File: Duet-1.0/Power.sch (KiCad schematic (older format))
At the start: 25 parts, among them J21 12V_ref, J30 5V_ref, J31 3v3_ref, U2 TC2117-3.3VDBTR, U3 MC7805CDTG

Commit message: Work-in-progress: Adding JMG's clean 5V buck converter.
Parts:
- removed U3: MC7805CDTG, symbol 7805
- added C96: 100u, symbol C
- added D19: SS14M, symbol DIODESCH
- added L1: L_MINI, ~, symbol L_MINI
- added U3: LM2596, symbol LM2596
- C3: value 100u -> 470u
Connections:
- wire segments 55 -> 60
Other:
- note added: "12-24V Input, 5V 2A Output buck converter\n"
- note removed: "12-24V Input, 5V 1A Output 7805 regulator\n"
- moved on the sheet: C3, C5, D1, D13, D14, D2, JP1, JP9
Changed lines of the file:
@@
 LIBS:FE
 LIBS:Shield-cache
+LIBS:emaker
+LIBS:SparkFun
 LIBS:Duet1.0-cache
 EELAYER 27 0
@@
 Wire Wire Line
 	6000 4900 6000 4800
-Connection ~ 5250 1800
-Wire Wire Line
-	5250 1800 5250 1900
-Wire Wire Line
-	4100 2100 4100 2200
-Wire Wire Line
-	2600 1800 2250 1800
+Connection ~ 6150 1800
+Wire Wire Line
+	6150 1800 6150 1900
 Wire Wire Line
 	6600 4450 6600 4050
@@
 Wire Notes Line
 	5000 3650 7000 3650
-Wire Wire Line
-	5950 1300 5700 1300
-Connection ~ 5700 1800
-Wire Wire Line
-	5700 1300 5700 1800
 Wire Wire Line
 	2000 5450 2000 5550
@@
 Connection ~ 3250 4250
 Wire Wire Line
-	5250 2550 5250 2300
-Wire Wire Line
-	3200 2200 3200 3000
+	6150 2550 6150 2300
+Wire Wire Line
+	2500 2200 2500 3000
 Wire Wire Line
 	6600 5500 6600 5150
-Wire Wire Line
-	4600 1800 4500 1800
 Wire Wire Line
 	6150 4800 5850 4800
@@
 	6000 5400 6600 5400
 Connection ~ 6600 5400
-Connection ~ 3200 2800
 Wire Wire Line
 	2150 5000 2150 5450
@@
 Connection ~ 4250 4250
 Wire Wire Line
-	1750 1800 1850 1800
-Connection ~ 1800 1800
-Wire Wire Line
-	4100 2200 3200 2200
-Connection ~ 3550 2200
-Wire Wire Line
-	3700 1800 3200 1800
-Connection ~ 3550 1800
+	1650 2300 1650 2200
+Connection ~ 1650 2250
+Connection ~ 2850 1800
 $Comp
 L C C95
@@
 L CP1 C5
 U 1 1 53B02FA8
-P 3550 2000
-F 0 "C5" H 3600 2100 50  0000 L CNN
-F 1 "0u33" H 3600 1900 50  0000 L CNN
-F 2 "" H 3550 2000 60  0001 C CNN
-F 3 "" H 3550 2000 60  0001 C CNN
-	1    3550 2000
+P 2850 2000
+F 0 "C5" H 2900 2100 50  0000 L CNN
+F 1 "0u33" H 2900 1900 50  0000 L CNN
+F 2 "" H 2850 2000 60  0001 C CNN
+F 3 "" H 2850 2000 60  0001 C CNN
+	1    2850 2000
 	1    0    0    -1
 $EndComp
@@
 L DIODESCH D2
 U 1 1 53B02782
-P 4800 1800
-F 0 "D2" H 4800 1900 40  0000 C CNN
-F 1 "SS14M" H 4800 1700 40  0000 C CNN
-F 2 "" H 4800 1800 60  0001 C CNN
-F 3 "" H 4800 1800 60  0001 C CNN
-	1    4800 1800
-	1    0    0    -1
-$EndComp
-$Comp
-L 7805 U3
-U 1 1 53B01DB6
-P 4100 1850
-F 0 "U3" H 4250 1654 60  0000 C CNN
-F 1 "MC7805CDTG" H 4100 2050 60  0000 C CNN
-F 2 "" H 4100 1850 60  0001 C CNN
-F 3 "" H 4100 1850 60  0001 C CNN
-	1    4100 1850
+P 5850 1800
+F 0 "D2" H 5850 1900 40  0000 C CNN
+F 1 "SS14M" H 5850 1700 40  0000 C CNN
+F 2 "" H 5850 1800 60  0001 C CNN
+F 3 "" H 5850 1800 60  0001 C CNN
+	1    5850 1800
 	1    0    0    -1
 $EndComp
@@
 Text GLabel 6150 4050 0    60   Input ~ 0
 PS_ON_IN
-Text Notes 5400 2150 0    60   ~ 0
+Text Notes 6300 2150 0    60   ~ 0
 1A
 Text Notes 6000 3250 0    60   ~ 0
@@
 L JUMPER JP9
 U 1 1 52209EAB
-P 2900 1800
-F 0 "JP9" H 2900 1950 60  0000 C CNN
-F 1 "5V_EN" H 2900 1720 40  0000 C CNN
-F 2 "" H 2900 1800 60  0001 C CNN
-F 3 "" H 2900 1800 60  0001 C CNN
-	1    2900 1800
+P 2100 1800
+F 0 "JP9" H 2100 1950 60  0000 C CNN
+F 1 "5V_EN" H 2100 1720 40  0000 C CNN
+F 2 "" H 2100 1800 60  0001 C CNN
+F 3 "" H 2100 1800 60  0001 C CNN
+	1    2100 1800
 	1    0    0    -1
 $EndComp
@@
 L SS3P4 D1
 U 1 1 5116BBAA
-P 2050 1800
-F 0 "D1" H 2050 1900 40  0000 C CNN
-F 1 "SS3P4" H 2050 1700 40  0000 C CNN
-F 2 "" H 2050 1800 60  0001 C CNN
-F 3 "" H 2050 1800 60  0001 C CNN
-	1    2050 1800
-	1    0    0    -1
+P 1650 2000
+F 0 "D1" H 1650 2100 40  0000 C CNN
+F 1 "SS3P4" H 1650 1900 40  0000 C CNN
+F 2 "" H 1650 2000 60  0001 C CNN
+F 3 "" H 1650 2000 60  0001 C CNN
+	1    1650 2000
+	0    -1   -1   0
 $EndComp
 $Comp
 L DIODESCH D13
 U 1 1 50F99BAC
-P 5250 2100
-F 0 "D13" H 5250 2200 40  0000 C CNN
-F 1 "SS14M" H 5250 2000 40  0000 C CNN
-F 2 "" H 5250 2100 60  0001 C CNN
-F 3 "" H 5250 2100 60  0001 C CNN
-	1    5250 2100
+P 6150 2100
+F 0 "D13" H 6150 2200 40  0000 C CNN
+F 1 "SS14M" H 6150 2000 40  0000 C CNN
+F 2 "" H 6150 2100 60  0001 C CNN
+F 3 "" H 6150 2100 60  0001 C CNN
+	1    6150 2100
 	0    -1   -1   0
 $EndComp
-Text GLabel 5250 2550 3    60   Input ~ 0
+Text GLabel 6150 2550 3    60   Input ~ 0
 VBUS
 $Comp
@@
 5V Input, 3.3V 500mA Output\nLow Drop-Out Linear Regulator
 Text Notes 1500 1300 0    60   ~ 0
-12-24V Input, 5V 1A Output 7805 regulator\n
+12-24V Input, 5V 2A Output buck converter\n
 Text GLabel 4350 4250 2    60   Input ~ 0
 +3.3V
 Text GLabel 1800 4250 0    60   Input ~ 0
 +5V
-Text GLabel 1750 1800 0    60   Input ~ 0
+Text GLabel 1650 2300 3    60   Input ~ 0
 V_IN
-Text GLabel 5950 1300 2    60   Input ~ 0
+Text GLabel 6650 1300 2    60   Input ~ 0
 +5V
 $Comp
@@
 L GND #PWR31
 U 1 1 50522566
-P 3200 3000
-F 0 "#PWR31" H 3200 3000 30  0001 C CNN
-F 1 "GND" H 3200 2930 30  0001 C CNN
-F 2 "" H 3200 3000 60  0001 C CNN
-F 3 "" H 3200 3000 60  0001 C CNN
-	1    3200 3000
+P 2500 3000
+F 0 "#PWR31" H 2500 3000 30  0001 C CNN
+F 1 "GND" H 2500 2930 30  0001 C CNN
+F 2 "" H 2500 3000 60  0001 C CNN
+F 3 "" H 2500 3000 60  0001 C CNN
+	1    2500 3000
 	1    0    0    -1
 $EndComp
@@
 L C C3
 U 1 1 50522565
-P 3200 2000
-F 0 "C3" H 3250 2100 50  0000 L CNN
-F 1 "100u" H 3250 1900 50  0000 L CNN
-F 2 "" H 3200 2000 60  0001 C CNN
-F 3 "" H 3200 2000 60  0001 C CNN
-F 4 "35V" H 3250 1830 50  0000 L CNN "Voltage"
-	1    3200 2000
+P 2500 2000
+F 0 "C3" H 2550 2100 50  0000 L CNN
+F 1 "470u" H 2550 1900 50  0000 L CNN
+F 2 "" H 2500 2000 60  0001 C CNN
+F 3 "" H 2500 2000 60  0001 C CNN
+F 4 "35V" H 2550 1830 50  0000 L CNN "Voltage"
+	1    2500 2000
 	1    0    0    -1
 $EndComp
@@
 Wire Wire Line
 	2000 5450 3850 5450
-Wire Wire Line
-	5000 1800 5900 1800
-Text Notes 6700 2200 0    60   ~ 0
+Text Notes 7100 2200 0    60   ~ 0
 1A
 $Comp
 L DIODESCH D14
 U 1 1 55096BA8
-P 6550 2150
-F 0 "D14" H 6550 2250 40  0000 C CNN
-F 1 "SS14M" H 6550 2050 40  0000 C CNN
-F 2 "" H 6550 2150 60  0001 C CNN
-F 3 "" H 6550 2150 60  0001 C CNN
-	1    6550 2150
+P 6950 2150
+F 0 "D14" H 6950 2250 40  0000 C CNN
+F 1 "SS14M" H 6950 2050 40  0000 C CNN
+F 2 "" H 6950 2150 60  0001 C CNN
+F 3 "" H 6950 2150 60  0001 C CNN
+	1    6950 2150
 	0    -1   -1   0
 $EndComp
-Text GLabel 6550 2450 3    60   Input ~ 0
+Text GLabel 6950 2450 3    60   Input ~ 0
 5V_IN
 Wire Wire Line
-	6550 2450 6550 2350
+	6950 2450 6950 2350
 $Comp
 L JUMPER JP1
 U 1 1 55096BFF
-P 6200 1800
-F 0 "JP1" H 6200 1950 60  0000 C CNN
-F 1 "EXT_5V_EN" H 6200 1720 40  0000 C CNN
-F 2 "" H 6200 1800 60  0001 C CNN
-F 3 "" H 6200 1800 60  0001 C CNN
-	1    6200 1800
-	1    0    0    -1
-$EndComp
-Wire Wire Line
-	6550 1950 6550 1800
-Wire Wire Line
-	6550 1800 6500 1800
+P 6600 1800
+F 0 "JP1" H 6600 1950 60  0000 C CNN
+F 1 "EXT_5V_EN" H 6600 1720 40  0000 C CNN
+F 2 "" H 6600 1800 60  0001 C CNN
+F 3 "" H 6600 1800 60  0001 C CNN
+	1    6600 1800
+	1    0    0    -1
+$EndComp
+Wire Wire Line
+	6950 1950 6950 1800
+Wire Wire Line
+	6950 1800 6900 1800
 $Comp
 L VREF J31
@@
 Wire Wire Line
 	9000 1800 9100 1800
+Wire Wire Line
+	2400 1800 3150 1800
+Wire Wire Line
+	1650 1800 1800 1800
+Connection ~ 2500 1800
+$Comp
+L C C96
+U 1 1 55CDF7BB
+P 5550 2000
+F 0 "C96" H 5600 2100 50  0000 L CNN
+F 1 "100u" H 5600 1900 50  0000 L CNN
+F 2 "" H 5550 2000 60  0001 C CNN
+F 3 "" H 5550 2000 60  0001 C CNN
+F 4 "35V" H 5600 1830 50  0000 L CNN "Voltage"
+	1    5550 2000
+	1    0    0    -1
+$EndComp
+$Comp
+L LM2596 U3
+U 1 1 55CDF7DB
+P 3850 2050
+F 0 "U3" H 3850 2150 50  0000 C CNN
+F 1 "LM2596" H 3850 2050 50  0000 C CNN
+F 2 "" H 3850 2550 60  0000 C CNN
+F 3 "" H 3850 2550 60  0000 C CNN
+	1    3850 2050
+	1    0    0    -1
+$EndComp
+Wire Wire Line
+	6650 1300 6300 1300
+Wire Wire Line
+	6300 1300 6300 1800
+Wire Wire Line
+	6300 1800 6050 1800
+Connection ~ 6300 1800
+Wire Wire Line
+	4550 1800 5650 1800
+Wire Wire Line
+	5550 2650 5550 2200
+Wire Wire Line
+	2500 2650 5550 2650
+Connection ~ 2500 2650
+Connection ~ 3550 2650
+$Comp
+L L_MINI L1
+U 1 1 55CDFB01
+P 4950 2200
+F 0 "L1" H 4875 2150 30  0000 C CNN
+F 1 "L_MINI" H 4950 2250 22  0000 C CNN
+F 2 "~" H 4950 2200 60  0000 C CNN
+F 3 "~" H 4950 2200 60  0000 C CNN
+	1    4950 2200
+	1    0    0    -1
+$EndComp
+$Comp
+L DIODESCH D19
+U 1 1 55CDFB0E
+P 4700 2400
+F 0 "D19" H 4700 2500 40  0000 C CNN
+F 1 "SS14M" H 4700 2300 40  0000 C CNN
+F 2 "" H 4700 2400 60  0001 C CNN
+F 3 "" H 4700 2400 60  0001 C CNN
+	1    4700 2400
+	0    -1   -1   0
+$EndComp
+Wire Wire Line
+	4550 2200 4850 2200
+Connection ~ 4700 2200
+Wire Wire Line
+	4700 2650 4700 2600
+Connection ~ 4200 2650
+Wire Wire Line
+	5050 2200 5300 2200
+Wire Wire Line
+	5300 2200 5300 1800
+Connection ~ 5550 1800
+Connection ~ 5300 1800
+Connection ~ 4700 2650
+Wire Wire Line
+	2850 2200 2850 2650
+Connection ~ 2850 2650
 $EndSCHEMATC

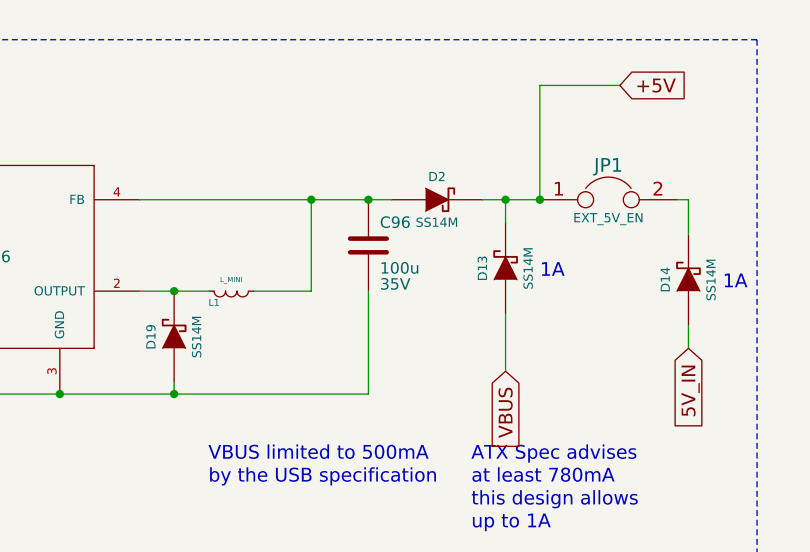
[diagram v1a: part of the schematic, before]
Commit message: Buck converter layout modified to fatten tracks and enhance grounds.
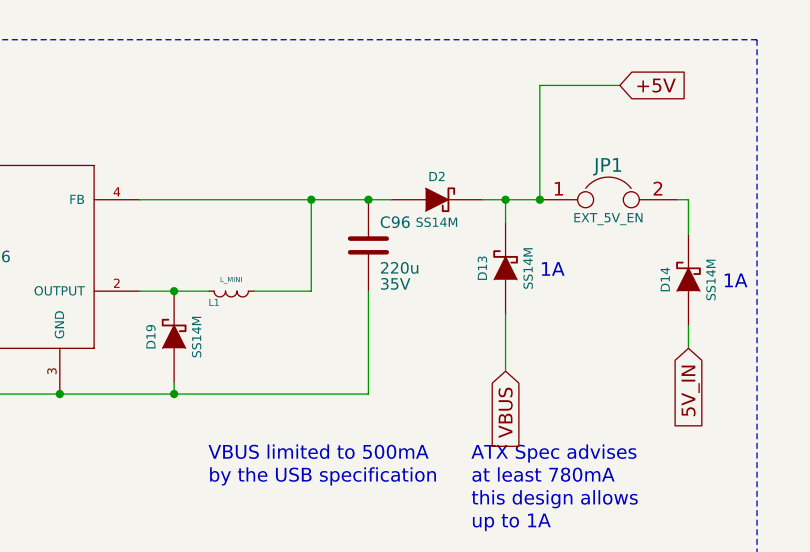
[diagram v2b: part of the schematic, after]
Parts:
- C96: value 100u -> 220u
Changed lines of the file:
@@
 Sheet 3 7
 Title "Duet"
-Date "14 aug 2015"
+Date "27 aug 2015"
 Rev "0.7"
 Comp "Think3DPrint3D, RepRapPro"
@@
 P 5550 2000
 F 0 "C96" H 5600 2100 50  0000 L CNN
-F 1 "100u" H 5600 1900 50  0000 L CNN
+F 1 "220u" H 5600 1900 50  0000 L CNN
 F 2 "" H 5550 2000 60  0001 C CNN
 F 3 "" H 5550 2000 60  0001 C CNN

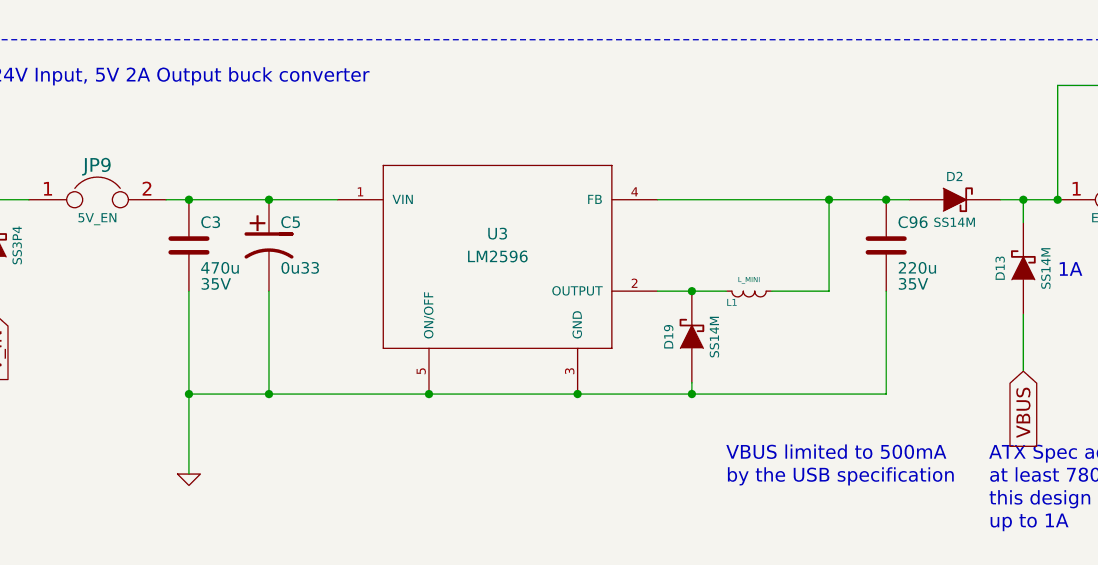
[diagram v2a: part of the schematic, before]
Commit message: Making 5V buck using more readily available components; also smaller ones to fit them in.
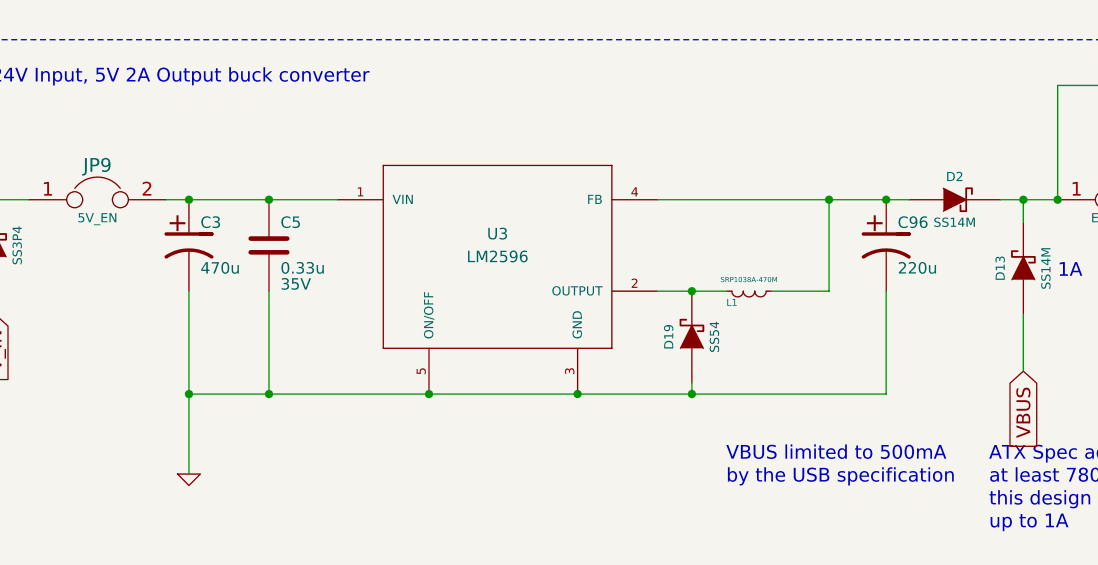
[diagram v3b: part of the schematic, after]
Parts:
- removed C3: 470u, symbol C
- removed C5: 0u33, symbol CP1
- removed C96: 220u, symbol C
- added C3: 470u, symbol CP1
- added C5: 0.33u, symbol C
- added C96: 220u, symbol CP1
- D19: value SS14M -> SS54
- L1: value L_MINI -> SRP1038A-470M
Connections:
- net GND: now also C3.2, C5.2, C96.2
- net at JP9.2, U3.1 (VIN): now also C3.1, C5.1
- net at D2.1 (A), L1.2 (B), U3.4 (FB): now also C96.1
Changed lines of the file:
@@
 Sheet 3 7
 Title "Duet"
-Date "27 aug 2015"
+Date "8 oct 2015"
 Rev "0.7"
 Comp "Think3DPrint3D, RepRapPro"
@@
 $EndComp
 $Comp
-L CP1 C5
-U 1 1 53B02FA8
-P 2850 2000
-F 0 "C5" H 2900 2100 50  0000 L CNN
-F 1 "0u33" H 2900 1900 50  0000 L CNN
-F 2 "" H 2850 2000 60  0001 C CNN
-F 3 "" H 2850 2000 60  0001 C CNN
-	1    2850 2000
-	1    0    0    -1
-$EndComp
-$Comp
 L CP1 C4
 U 1 1 53B02AAB
@@
 PS_ON Control
 $Comp
-L GND #PWR32
+L GND #PWR030
 U 1 1 5220BA8F
 P 6600 5500
-F 0 "#PWR32" H 6600 5500 30  0001 C CNN
+F 0 "#PWR030" H 6600 5500 30  0001 C CNN
 F 1 "GND" H 6600 5430 30  0001 C CNN
 F 2 "" H 6600 5500 60  0001 C CNN
@@
 +5V
 $Comp
-L GND #PWR30
+L GND #PWR031
 U 1 1 50522574
 P 2000 5550
-F 0 "#PWR30" H 2000 5550 30  0001 C CNN
+F 0 "#PWR031" H 2000 5550 30  0001 C CNN
 F 1 "GND" H 2000 5480 30  0001 C CNN
 F 2 "" H 2000 5550 60  0001 C CNN
@@
 $EndComp
 $Comp
-L GND #PWR31
+L GND #PWR032
 U 1 1 50522566
 P 2500 3000
-F 0 "#PWR31" H 2500 3000 30  0001 C CNN
+F 0 "#PWR032" H 2500 3000 30  0001 C CNN
 F 1 "GND" H 2500 2930 30  0001 C CNN
 F 2 "" H 2500 3000 60  0001 C CNN
 F 3 "" H 2500 3000 60  0001 C CNN
 	1    2500 3000
-	1    0    0    -1
-$EndComp
-$Comp
-L C C3
-U 1 1 50522565
-P 2500 2000
-F 0 "C3" H 2550 2100 50  0000 L CNN
-F 1 "470u" H 2550 1900 50  0000 L CNN
-F 2 "" H 2500 2000 60  0001 C CNN
-F 3 "" H 2500 2000 60  0001 C CNN
-F 4 "35V" H 2550 1830 50  0000 L CNN "Voltage"
-	1    2500 2000
 	1    0    0    -1
 $EndComp
@@
 +3.3V
 $Comp
-L GND #PWR33
+L GND #PWR033
 U 1 1 54EF3E25
 P 8650 3000
-F 0 "#PWR33" H 8650 3000 30  0001 C CNN
+F 0 "#PWR033" H 8650 3000 30  0001 C CNN
 F 1 "GND" H 8650 2930 30  0001 C CNN
 F 2 "" H 8650 3000 60  0001 C CNN
@@
 Connection ~ 2500 1800
 $Comp
-L C C96
-U 1 1 55CDF7BB
-P 5550 2000
-F 0 "C96" H 5600 2100 50  0000 L CNN
-F 1 "220u" H 5600 1900 50  0000 L CNN
-F 2 "" H 5550 2000 60  0001 C CNN
-F 3 "" H 5550 2000 60  0001 C CNN
-F 4 "35V" H 5600 1830 50  0000 L CNN "Voltage"
-	1    5550 2000
-	1    0    0    -1
-$EndComp
-$Comp
 L LM2596 U3
 U 1 1 55CDF7DB
@@
 P 4950 2200
 F 0 "L1" H 4875 2150 30  0000 C CNN
-F 1 "L_MINI" H 4950 2250 22  0000 C CNN
+F 1 "SRP1038A-470M" H 4950 2250 22  0000 C CNN
 F 2 "~" H 4950 2200 60  0000 C CNN
 F 3 "~" H 4950 2200 60  0000 C CNN
@@
 P 4700 2400
 F 0 "D19" H 4700 2500 40  0000 C CNN
-F 1 "SS14M" H 4700 2300 40  0000 C CNN
+F 1 "SS54" H 4700 2300 40  0000 C CNN
 F 2 "" H 4700 2400 60  0001 C CNN
 F 3 "" H 4700 2400 60  0001 C CNN
@@
 	2850 2200 2850 2650
 Connection ~ 2850 2650
+$Comp
+L C C5
+U 1 1 56164E62
+P 2850 2000
+F 0 "C5" H 2900 2100 50  0000 L CNN
+F 1 "0.33u" H 2900 1900 50  0000 L CNN
+F 2 "" H 2850 2000 60  0001 C CNN
+F 3 "" H 2850 2000 60  0001 C CNN
+F 4 "35V" H 2900 1830 50  0000 L CNN "Voltage"
+	1    2850 2000
+	1    0    0    -1
+$EndComp
+$Comp
+L CP1 C3
+U 1 1 56164E6E
+P 2500 2000
+F 0 "C3" H 2550 2100 50  0000 L CNN
+F 1 "470u" H 2550 1900 50  0000 L CNN
+F 2 "" H 2500 2000 60  0001 C CNN
+F 3 "" H 2500 2000 60  0001 C CNN
+	1    2500 2000
+	1    0    0    -1
+$EndComp
+$Comp
+L CP1 C96
+U 1 1 56164E74
+P 5550 2000
+F 0 "C96" H 5600 2100 50  0000 L CNN
+F 1 "220u" H 5600 1900 50  0000 L CNN
+F 2 "" H 5550 2000 60  0001 C CNN
+F 3 "" H 5550 2000 60  0001 C CNN
+	1    5550 2000
+	1    0    0    -1
+$EndComp
 $EndSCHEMATC

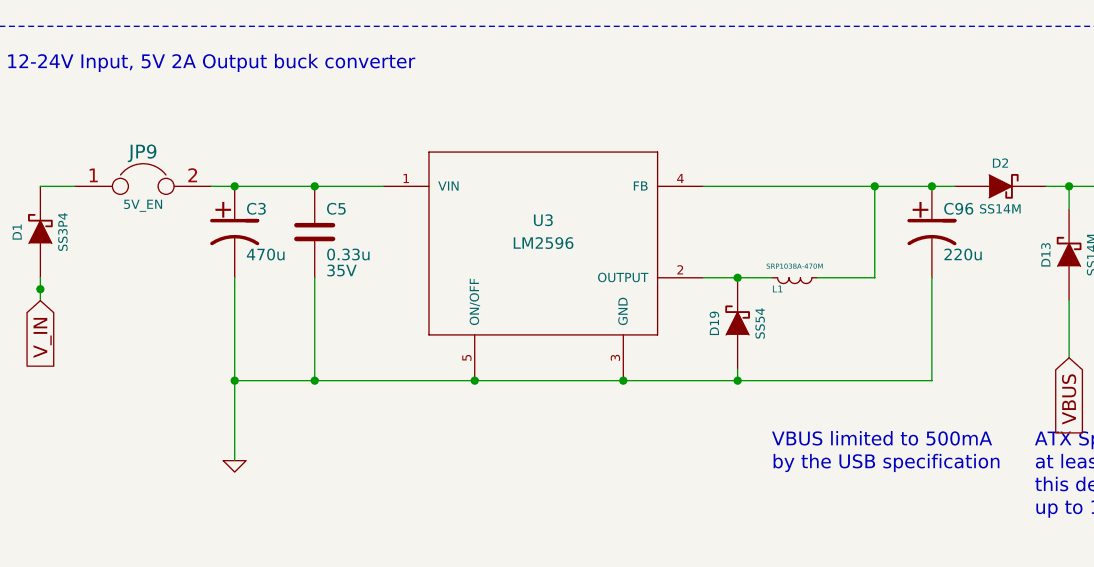
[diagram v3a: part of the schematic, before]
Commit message: 470uF cap on 5v buck converter replaced by 2 x 220uF.
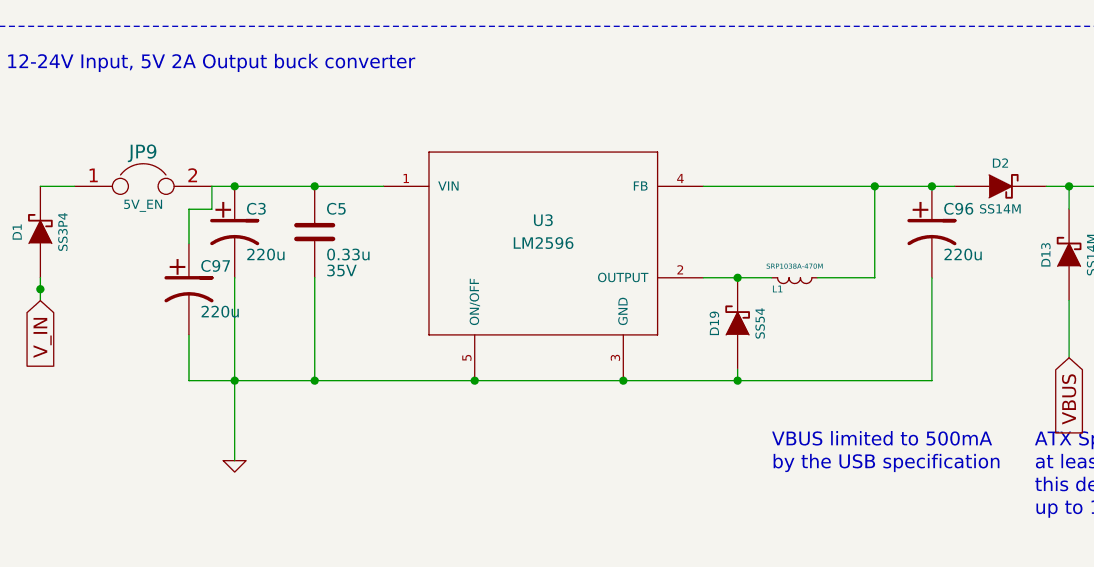
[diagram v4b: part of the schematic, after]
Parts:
- added C97: 220u, symbol CP1
- C3: value 470u -> 220u
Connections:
- net GND: now also C97.2
- net at C3.1, C5.1, JP9.2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: now also C97.1
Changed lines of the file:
@@
 Sheet 3 7
 Title "Duet"
-Date "8 oct 2015"
+Date "17 oct 2015"
 Rev "0.7"
 Comp "Think3DPrint3D, RepRapPro"
@@
 	5550 2650 5550 2200
 Wire Wire Line
-	2500 2650 5550 2650
+	2300 2650 5550 2650
 Connection ~ 2500 2650
 Connection ~ 3550 2650
@@
 P 2500 2000
 F 0 "C3" H 2550 2100 50  0000 L CNN
-F 1 "470u" H 2550 1900 50  0000 L CNN
+F 1 "220u" H 2550 1900 50  0000 L CNN
 F 2 "" H 2500 2000 60  0001 C CNN
 F 3 "" H 2500 2000 60  0001 C CNN
@@
 	1    0    0    -1
 $EndComp
+$Comp
+L CP1 C97
+U 1 1 56226C3D
+P 2300 2250
+F 0 "C97" H 2350 2350 50  0000 L CNN
+F 1 "220u" H 2350 2150 50  0000 L CNN
+F 2 "" H 2300 2250 60  0001 C CNN
+F 3 "" H 2300 2250 60  0001 C CNN
+	1    2300 2250
+	1    0    0    -1
+$EndComp
+Wire Wire Line
+	2300 2650 2300 2450
+Wire Wire Line
+	2300 2050 2300 1900
+Wire Wire Line
+	2300 1900 2400 1900
+Wire Wire Line
+	2400 1900 2400 1800
 $EndSCHEMATC
